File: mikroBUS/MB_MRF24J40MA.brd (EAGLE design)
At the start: 51.7 x 33 mm, 2 parts

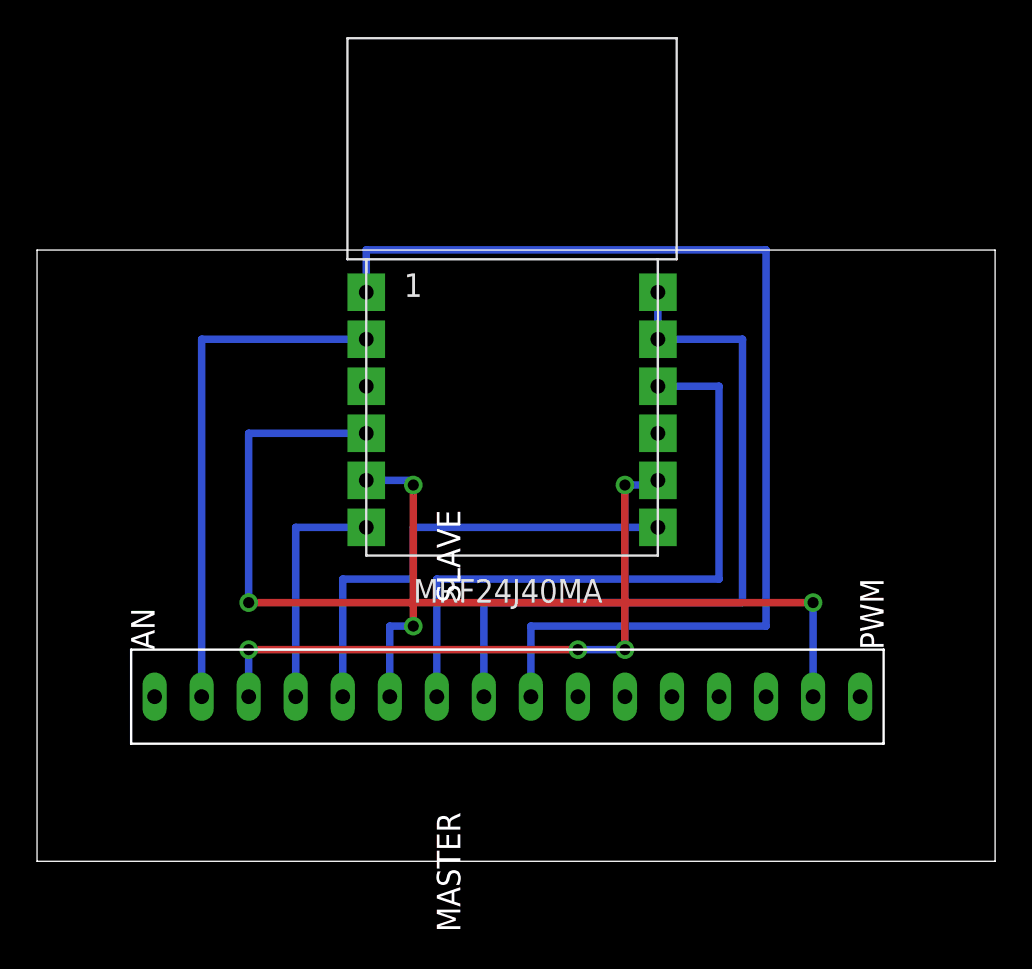
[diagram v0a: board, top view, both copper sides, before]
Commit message: 
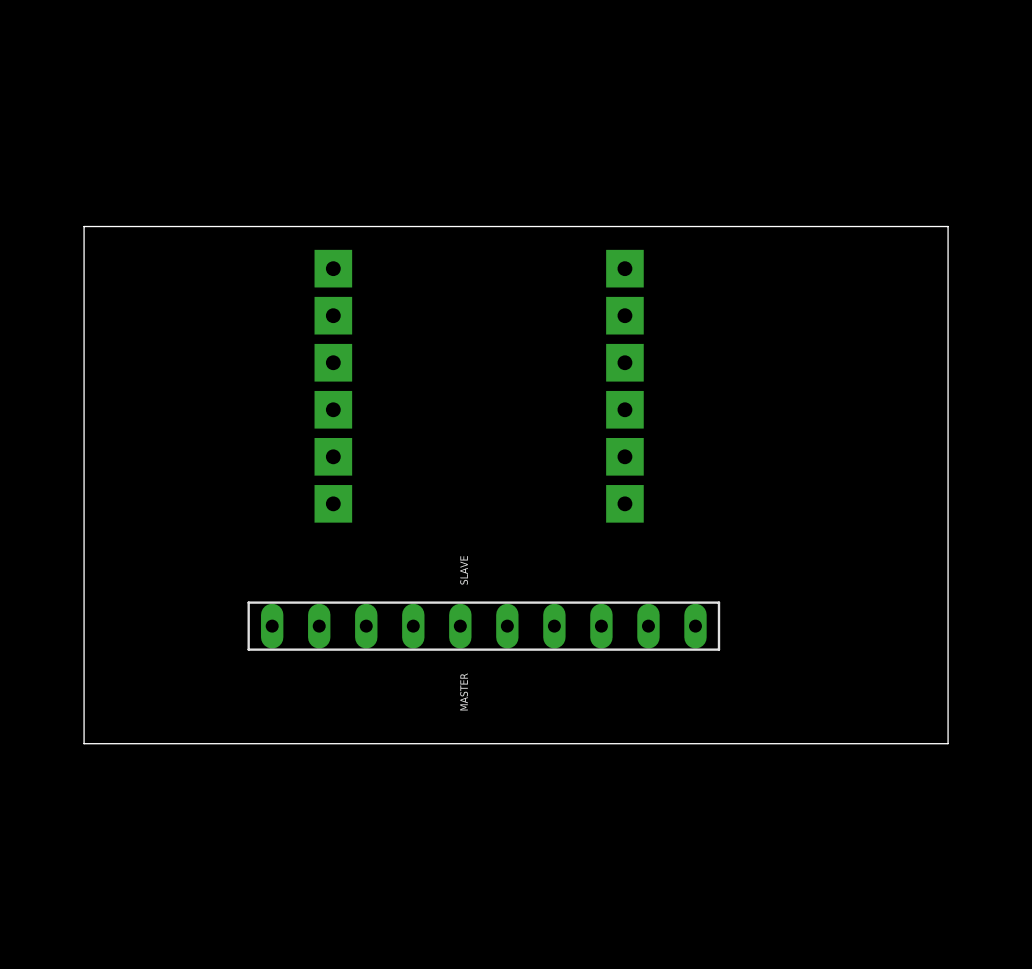
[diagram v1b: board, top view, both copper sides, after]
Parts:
- removed U$2: (no value), lieven:MIKROBUS_SIL
- added U$3: SPI_BUS, lieven:SPI_BUS
- moved U$1 14.0 mm to (50.8, 17.8), flipped to the bottom
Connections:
- net N$1: now also U$1.GND, U$1.GND1, U$1.GND2, U$3.GND; no longer U$1.INT, U$2.INT
- net N$2: now also U$1.VIN, U$3.+3V3; no longer U$1.GND, U$2.GND2
- net N$3: now also U$1.SDI, U$3.MOSI; no longer U$1.RESET, U$2.RST
- net N$4: now also U$1.SDO, U$3.MISO; no longer U$1.CS(LOW), U$2.CS
- net N$5: now also U$3.SCK; no longer U$2.SCK
- net N$6: now also U$1.CS(LOW), U$3.CS; no longer U$1.SDO, U$2.MISO
- net N$7: now also U$1.INT, U$3.INT; no longer U$1.SDI, U$2.MOSI
- net N$8: now also U$1.RESET, U$3.RST; no longer U$1.VIN, U$2.+3.3V
- net N$9: now also U$1.WAKE, U$3.GPIO; no longer U$1.GND1, U$1.GND2, U$2.GND
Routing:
- net N$2: track 60.7 -> 0.00 mm
- net N$1: track 51.1 -> 0.00 mm, vias 2 -> 0
- net N$9: track 40.4 -> 0.00 mm
- net N$8: track 35.3 -> 0.00 mm
- net N$4: track 33.8 -> 0.00 mm, vias 4 -> 0
- net N$3: track 28.2 -> 0.00 mm
- net N$6: track 26.2 -> 0.00 mm
- net N$7: track 15.5 -> 0.00 mm, vias 2 -> 0
- net N$5: track 13.0 -> 0.00 mm
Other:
- board size 51.7 x 33 mm -> 46.7 x 27.9 mm
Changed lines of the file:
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@@
 <board>
 <plain>
-<wire x1="19.05" y1="0" x2="70.79" y2="0" width="0" layer="20"/>
-<wire x1="70.79" y1="0" x2="70.79" y2="33.01" width="0" layer="20"/>
-<wire x1="70.79" y1="33.01" x2="19.05" y2="33.01" width="0" layer="20"/>
-<wire x1="19.05" y1="33.01" x2="19.05" y2="0" width="0" layer="20"/>
+<wire x1="21.59" y1="6.35" x2="68.25" y2="6.35" width="0" layer="20"/>
+<wire x1="68.25" y1="6.35" x2="68.25" y2="34.28" width="0" layer="20"/>
+<wire x1="68.25" y1="34.28" x2="21.59" y2="34.28" width="0" layer="20"/>
+<wire x1="21.59" y1="34.28" x2="21.59" y2="6.35" width="0" layer="20"/>
 </plain>
 <attributes>
@@
 </autorouter>
 <elements>
-<element name="U$1" library="lieven" package="MRF24J40MA" value="MRF24J40MA" x="36.83" y="16.51"/>
-<element name="U$2" library="lieven" package="MIKROBUS_SIL" value="" x="43.18" y="8.89" rot="R90"/>
+<element name="U$1" library="lieven" package="MRF24J40MA" value="MRF24J40MA" x="50.8" y="17.78" rot="MR0"/>
+<element name="U$3" library="lieven" package="SPI_BUS" value="SPI_BUS" x="31.75" y="12.7" rot="R270"/>
 </elements>
 <signals>
 <signal name="N$1">
-<contactref element="U$1" pad="INT"/>
-<contactref element="U$2" pad="INT"/>
-<wire x1="36.83" y1="23.114" x2="30.48" y2="23.114" width="0.4064" layer="16"/>
-<wire x1="30.48" y1="23.114" x2="30.48" y2="13.97" width="0.4064" layer="16"/>
-<via x="30.48" y="13.97" extent="1-16" drill="0.6" shape="square"/>
-<wire x1="30.48" y1="13.97" x2="60.96" y2="13.97" width="0.4064" layer="1"/>
-<via x="60.96" y="13.97" extent="1-16" drill="0.6" shape="square"/>
-<wire x1="60.96" y1="13.97" x2="60.96" y2="8.89" width="0.4064" layer="16"/>
+<contactref element="U$1" pad="GND"/>
+<contactref element="U$3" pad="GND"/>
+<contactref element="U$1" pad="GND2"/>
+<contactref element="U$1" pad="GND1"/>
+<wire x1="35.052" y1="32.004" x2="50.8" y2="32.004" width="0" layer="19" extent="1-1"/>
+<wire x1="35.052" y1="29.464" x2="35.052" y2="32.004" width="0" layer="19" extent="1-1"/>
+<wire x1="31.75" y1="12.7" x2="35.052" y2="29.464" width="0" layer="19" extent="1-1"/>
 </signal>
 <signal name="N$2">
-<contactref element="U$1" pad="GND"/>
-<contactref element="U$2" pad="GND2"/>
-<wire x1="45.72" y1="8.89" x2="45.72" y2="12.7" width="0.4064" layer="16"/>
-<wire x1="45.72" y1="12.7" x2="58.42" y2="12.7" width="0.4064" layer="16"/>
-<wire x1="58.42" y1="12.7" x2="58.42" y2="33.02" width="0.4064" layer="16"/>
-<wire x1="58.42" y1="33.02" x2="36.83" y2="33.02" width="0.4064" layer="16"/>
-<wire x1="36.83" y1="33.02" x2="36.83" y2="30.734" width="0.4064" layer="16"/>
+<contactref element="U$1" pad="VIN"/>
+<contactref element="U$3" pad="+3V3"/>
+<wire x1="34.29" y1="12.7" x2="35.052" y2="26.924" width="0" layer="19" extent="1-1"/>
 </signal>
 <signal name="N$3">
-<contactref element="U$1" pad="RESET"/>
-<contactref element="U$2" pad="RST"/>
-<wire x1="36.83" y1="28.194" x2="27.94" y2="28.194" width="0.4064" layer="16"/>
-<wire x1="27.94" y1="28.194" x2="27.94" y2="8.89" width="0.4064" layer="16"/>
+<contactref element="U$1" pad="SDI"/>
+<contactref element="U$3" pad="MOSI"/>
+<wire x1="39.37" y1="12.7" x2="50.8" y2="21.844" width="0" layer="19" extent="1-1"/>
 </signal>
 <signal name="N$4">
-<contactref element="U$1" pad="CS(LOW)"/>
-<contactref element="U$2" pad="CS"/>
-<wire x1="30.48" y1="8.89" x2="30.48" y2="11.43" width="0.4064" layer="16"/>
-<via x="30.48" y="11.43" extent="1-16" drill="0.6" shape="square"/>
-<wire x1="30.48" y1="11.43" x2="48.26" y2="11.43" width="0.4064" layer="1"/>
-<via x="48.26" y="11.43" extent="1-16" drill="0.6" shape="square"/>
-<wire x1="48.26" y1="11.43" x2="50.8" y2="11.43" width="0.4064" layer="16"/>
-<via x="50.8" y="11.43" extent="1-16" drill="0.6" shape="square"/>
-<wire x1="50.8" y1="11.43" x2="50.8" y2="20.32" width="0.4064" layer="1"/>
-<via x="50.8" y="20.32" extent="1-16" drill="0.6" shape="square"/>
-<wire x1="50.8" y1="20.32" x2="52.578" y2="20.32" width="0.4064" layer="16"/>
-<wire x1="52.578" y1="20.32" x2="52.578" y2="20.574" width="0.4064" layer="16"/>
+<contactref element="U$1" pad="SDO"/>
+<contactref element="U$3" pad="MISO"/>
+<wire x1="41.91" y1="12.7" x2="35.052" y2="19.304" width="0" layer="19" extent="1-1"/>
 </signal>
 <signal name="N$5">
 <contactref element="U$1" pad="SCK"/>
-<contactref element="U$2" pad="SCK"/>
-<wire x1="36.83" y1="18.034" x2="33.02" y2="18.034" width="0.4064" layer="16"/>
-<wire x1="33.02" y1="18.034" x2="33.02" y2="8.89" width="0.4064" layer="16"/>
+<contactref element="U$3" pad="SCK"/>
+<wire x1="44.45" y1="12.7" x2="50.8" y2="19.304" width="0" layer="19" extent="1-1"/>
 </signal>
 <signal name="N$6">
-<contactref element="U$1" pad="SDO"/>
-<contactref element="U$2" pad="MISO"/>
-<wire x1="52.578" y1="18.034" x2="39.37" y2="18.034" width="0.4064" layer="16"/>
-<wire x1="39.37" y1="18.034" x2="39.37" y2="15.24" width="0.4064" layer="16"/>
-<wire x1="39.37" y1="15.24" x2="35.56" y2="15.24" width="0.4064" layer="16"/>
-<wire x1="35.56" y1="15.24" x2="35.56" y2="8.89" width="0.4064" layer="16"/>
+<contactref element="U$1" pad="CS(LOW)"/>
+<contactref element="U$3" pad="CS"/>
+<wire x1="46.99" y1="12.7" x2="35.052" y2="21.844" width="0" layer="19" extent="1-1"/>
 </signal>
 <signal name="N$7">
-<contactref element="U$1" pad="SDI"/>
-<contactref element="U$2" pad="MOSI"/>
-<wire x1="36.83" y1="20.574" x2="39.37" y2="20.574" width="0.4064" layer="16"/>
-<wire x1="39.37" y1="20.574" x2="39.37" y2="20.32" width="0.4064" layer="16"/>
-<via x="39.37" y="20.32" extent="1-16" drill="0.6" shape="square"/>
-<wire x1="39.37" y1="20.32" x2="39.37" y2="12.7" width="0.4064" layer="1"/>
-<via x="39.37" y="12.7" extent="1-16" drill="0.6" shape="square"/>
-<wire x1="39.37" y1="12.7" x2="38.1" y2="12.7" width="0.4064" layer="16"/>
-<wire x1="38.1" y1="12.7" x2="38.1" y2="8.89" width="0.4064" layer="16"/>
+<contactref element="U$1" pad="INT"/>
+<contactref element="U$3" pad="INT"/>
+<wire x1="49.53" y1="12.7" x2="50.8" y2="24.384" width="0" layer="19" extent="1-1"/>
 </signal>
 <signal name="N$8">
-<contactref element="U$1" pad="VIN"/>
-<contactref element="U$2" pad="+3.3V"/>
-<wire x1="52.578" y1="25.654" x2="55.88" y2="25.654" width="0.4064" layer="16"/>
-<wire x1="55.88" y1="25.654" x2="55.88" y2="15.24" width="0.4064" layer="16"/>
-<wire x1="55.88" y1="15.24" x2="40.64" y2="15.24" width="0.4064" layer="16"/>
-<wire x1="40.64" y1="15.24" x2="40.64" y2="8.89" width="0.4064" layer="16"/>
+<contactref element="U$1" pad="RESET"/>
+<contactref element="U$3" pad="RST"/>
+<wire x1="52.07" y1="12.7" x2="50.8" y2="29.464" width="0" layer="19" extent="1-1"/>
 </signal>
 <signal name="N$9">
-<contactref element="U$1" pad="GND1"/>
-<contactref element="U$2" pad="GND"/>
-<contactref element="U$1" pad="GND2"/>
-<wire x1="52.578" y1="28.194" x2="52.578" y2="30.734" width="0.4064" layer="16"/>
-<wire x1="52.578" y1="28.194" x2="57.15" y2="28.194" width="0.4064" layer="16"/>
-<wire x1="57.15" y1="28.194" x2="57.15" y2="13.97" width="0.4064" layer="16"/>
-<wire x1="57.15" y1="13.97" x2="43.18" y2="13.97" width="0.4064" layer="16"/>
-<wire x1="43.18" y1="13.97" x2="43.18" y2="8.89" width="0.4064" layer="16"/>
+<contactref element="U$1" pad="WAKE"/>
+<contactref element="U$3" pad="GPIO"/>
+<wire x1="54.61" y1="12.7" x2="50.8" y2="26.924" width="0" layer="19" extent="1-1"/>
 </signal>
 </signals>
